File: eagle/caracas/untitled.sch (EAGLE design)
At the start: 24 parts, among them IC1 4001N, Q1 IRLZ44Z, X1 22-23-2021, X2 22-23-2021, X3 22-23-2021, X4 22-23-2041, X5 22-23-2021, X6 22-23-2041

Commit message: Possibly last version of schematics.
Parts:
- removed R6, R7, R8: 330, rcl:R-EU_0207/10
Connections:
- net +5V_SW_GND: now also X4-1.S
- net GND: now also U$1G$2.P$1; no longer R6.2, R7.2, R8.2, X4-1.S
- net N$10: now also X4-4.S; no longer R8.1, X4-2.S
- net N$7: now also X4-2.S; no longer R6.1, X4-4.S
- net N$8: no longer R7.1
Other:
- moved on the sheet: X4-1, X4-2, X4-3, X4-4
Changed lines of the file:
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@@
 <class number="0" name="default" width="0" drill="0">
 </class>
-<class number="1" name="Ground" width="0.6096" drill="0">
+<class number="1" name="Ground" width="0.4064" drill="0">
 <clearance class="1" value="0.3048"/>
 </class>
@@
 <part name="R10" library="rcl" deviceset="R-EU_" device="0207/10" value="1k"/>
 <part name="R9" library="rcl" deviceset="R-EU_" device="0207/10" value="1k"/>
-<part name="R6" library="rcl" deviceset="R-EU_" device="0207/10" value="330"/>
-<part name="R7" library="rcl" deviceset="R-EU_" device="0207/10" value="330"/>
-<part name="R8" library="rcl" deviceset="R-EU_" device="0207/10" value="330"/>
 <part name="X2" library="con-molex" deviceset="22-23-2021" device=""/>
 <part name="X3" library="con-molex" deviceset="22-23-2021" device=""/>
@@
 <instance part="R10" gate="G$1" x="-38.1" y="27.94" rot="R180"/>
 <instance part="R9" gate="G$1" x="-38.1" y="25.4" rot="R180"/>
-<instance part="R6" gate="G$1" x="-114.3" y="20.32" rot="R180"/>
-<instance part="R7" gate="G$1" x="-114.3" y="22.86" rot="R180"/>
-<instance part="R8" gate="G$1" x="-114.3" y="25.4" rot="R180"/>
 <instance part="X2" gate="-1" x="-213.36" y="12.7" rot="R90"/>
 <instance part="X2" gate="-2" x="-210.82" y="12.7" rot="R90"/>
@@
 <instance part="X1" gate="-2" x="-220.98" y="-55.88" rot="R270"/>
 <instance part="X6" gate="-1" x="-45.72" y="48.26" rot="R90"/>
-<instance part="X4" gate="-2" x="-99.06" y="0" rot="R270"/>
-<instance part="X4" gate="-3" x="-101.6" y="0" rot="R270"/>
-<instance part="X4" gate="-4" x="-104.14" y="0" rot="R270"/>
-<instance part="X4" gate="-1" x="-203.2" y="-55.88" rot="R270"/>
+<instance part="X4" gate="-2" x="-111.76" y="20.32" rot="R180"/>
+<instance part="X4" gate="-3" x="-111.76" y="22.86" rot="R180"/>
+<instance part="X4" gate="-4" x="-111.76" y="25.4" rot="R180"/>
 <instance part="X6" gate="-4" x="-25.4" y="17.78" rot="R270"/>
 <instance part="X6" gate="-3" x="-27.94" y="17.78" rot="R270"/>
@@
 <instance part="T1" gate="G$1" x="-152.4" y="-22.86"/>
 <instance part="R2" gate="G$1" x="-165.1" y="-22.86"/>
+<instance part="X4" gate="-1" x="-111.76" y="17.78" rot="R180"/>
+<instance part="U$1" gate="G$2" x="-223.52" y="-58.42" rot="R270"/>
 </instances>
 <busses>
@@
 <segment>
 <pinref part="U$1" gate="G$1" pin="P$1"/>
-<wire x1="-228.6" y1="-53.34" x2="-220.98" y2="-53.34" width="0.1524" layer="91"/>
+<wire x1="-228.6" y1="-53.34" x2="-223.52" y2="-53.34" width="0.1524" layer="91"/>
 <pinref part="X3" gate="-1" pin="S"/>
+<wire x1="-223.52" y1="-53.34" x2="-220.98" y2="-53.34" width="0.1524" layer="91"/>
 <wire x1="-220.98" y1="-53.34" x2="-218.44" y2="-53.34" width="0.1524" layer="91"/>
 <wire x1="-218.44" y1="-53.34" x2="-210.82" y2="-53.34" width="0.1524" layer="91"/>
 <wire x1="-210.82" y1="-53.34" x2="-208.28" y2="-53.34" width="0.1524" layer="91"/>
-<wire x1="-208.28" y1="-53.34" x2="-203.2" y2="-53.34" width="0.1524" layer="91"/>
 <junction x="-208.28" y="-53.34"/>
 <pinref part="X3" gate="-2" pin="S"/>
@@
 <junction x="-220.98" y="-53.34"/>
 <pinref part="IC1" gate="P" pin="VSS"/>
-<wire x1="-198.12" y1="-53.34" x2="-203.2" y2="-53.34" width="0.1524" layer="91"/>
+<wire x1="-198.12" y1="-53.34" x2="-208.28" y2="-53.34" width="0.1524" layer="91"/>
 <wire x1="-198.12" y1="-30.48" x2="-198.12" y2="-53.34" width="0.1524" layer="91"/>
 <junction x="-198.12" y="-53.34"/>
-<pinref part="X4" gate="-1" pin="S"/>
-<junction x="-203.2" y="-53.34"/>
 <pinref part="SUPPLY2" gate="GND" pin="GND"/>
 <pinref part="D1" gate="1" pin="A"/>
@@
 <pinref part="Q1" gate="G$1" pin="S"/>
 <wire x1="-91.44" y1="-15.24" x2="-91.44" y2="-53.34" width="0.1524" layer="91"/>
-<wire x1="-91.44" y1="-53.34" x2="-134.62" y2="-53.34" width="0.1524" layer="91"/>
+<wire x1="-91.44" y1="-53.34" x2="-142.24" y2="-53.34" width="0.1524" layer="91"/>
 <junction x="-142.24" y="-53.34"/>
 <pinref part="T1" gate="G$1" pin="E"/>
-<wire x1="-134.62" y1="-53.34" x2="-142.24" y2="-53.34" width="0.1524" layer="91"/>
 <wire x1="-149.86" y1="-27.94" x2="-149.86" y2="-53.34" width="0.1524" layer="91"/>
 <junction x="-149.86" y="-53.34"/>
-<wire x1="-203.2" y1="-53.34" x2="-177.8" y2="-53.34" width="0.1524" layer="91"/>
+<wire x1="-198.12" y1="-53.34" x2="-177.8" y2="-53.34" width="0.1524" layer="91"/>
 <pinref part="MCP3008" gate="A" pin="DGND"/>
 <wire x1="-17.78" y1="2.54" x2="-22.86" y2="2.54" width="0.1524" layer="91"/>
@@
 <wire x1="-22.86" y1="-53.34" x2="-91.44" y2="-53.34" width="0.1524" layer="91"/>
 <junction x="-91.44" y="-53.34"/>
-<pinref part="R8" gate="G$1" pin="2"/>
-<wire x1="-119.38" y1="25.4" x2="-134.62" y2="25.4" width="0.1524" layer="91"/>
-<pinref part="R6" gate="G$1" pin="2"/>
-<wire x1="-119.38" y1="20.32" x2="-134.62" y2="20.32" width="0.1524" layer="91"/>
-<wire x1="-134.62" y1="20.32" x2="-134.62" y2="22.86" width="0.1524" layer="91"/>
-<wire x1="-134.62" y1="22.86" x2="-134.62" y2="25.4" width="0.1524" layer="91"/>
-<pinref part="R7" gate="G$1" pin="2"/>
-<wire x1="-119.38" y1="22.86" x2="-134.62" y2="22.86" width="0.1524" layer="91"/>
-<junction x="-134.62" y="22.86"/>
-<junction x="-134.62" y="20.32"/>
-<wire x1="-134.62" y1="20.32" x2="-134.62" y2="-53.34" width="0.1524" layer="91"/>
-<junction x="-134.62" y="-53.34"/>
+<pinref part="U$1" gate="G$2" pin="P$1"/>
+<junction x="-223.52" y="-53.34"/>
 </segment>
 </net>
@@
 <pinref part="Q1" gate="G$1" pin="D"/>
 <wire x1="-91.44" y1="17.78" x2="-91.44" y2="-5.08" width="0.1524" layer="91"/>
+<pinref part="X4" gate="-1" pin="S"/>
+<wire x1="-109.22" y1="17.78" x2="-91.44" y2="17.78" width="0.1524" layer="91"/>
+<junction x="-91.44" y="17.78"/>
 </segment>
 </net>
@@
 <segment>
 <pinref part="RASPBERRYPI" gate="A" pin="8"/>
-<wire x1="-81.28" y1="20.32" x2="-104.14" y2="20.32" width="0.1524" layer="91"/>
-<wire x1="-104.14" y1="20.32" x2="-109.22" y2="20.32" width="0.1524" layer="91"/>
-<wire x1="-104.14" y1="20.32" x2="-104.14" y2="2.54" width="0.1524" layer="91"/>
-<junction x="-104.14" y="20.32"/>
-<pinref part="R6" gate="G$1" pin="1"/>
+<wire x1="-81.28" y1="20.32" x2="-109.22" y2="20.32" width="0.1524" layer="91"/>
+<pinref part="X4" gate="-2" pin="S"/>
+</segment>
+</net>
+<net name="N$8" class="0">
+<segment>
+<pinref part="RASPBERRYPI" gate="A" pin="10"/>
+<wire x1="-81.28" y1="22.86" x2="-109.22" y2="22.86" width="0.1524" layer="91"/>
+<pinref part="X4" gate="-3" pin="S"/>
+</segment>
+</net>
+<net name="N$10" class="0">
+<segment>
+<pinref part="RASPBERRYPI" gate="A" pin="12"/>
+<wire x1="-81.28" y1="25.4" x2="-109.22" y2="25.4" width="0.1524" layer="91"/>
 <pinref part="X4" gate="-4" pin="S"/>
 </segment>
 </net>
-<net name="N$8" class="0">
-<segment>
-<pinref part="RASPBERRYPI" gate="A" pin="10"/>
-<wire x1="-81.28" y1="22.86" x2="-101.6" y2="22.86" width="0.1524" layer="91"/>
-<wire x1="-104.14" y1="22.86" x2="-101.6" y2="22.86" width="0.1524" layer="91"/>
-<wire x1="-101.6" y1="22.86" x2="-109.22" y2="22.86" width="0.1524" layer="91"/>
-<wire x1="-101.6" y1="22.86" x2="-101.6" y2="2.54" width="0.1524" layer="91"/>
-<junction x="-101.6" y="22.86"/>
-<pinref part="R7" gate="G$1" pin="1"/>
-<pinref part="X4" gate="-3" pin="S"/>
-</segment>
-</net>
-<net name="N$10" class="0">
-<segment>
-<pinref part="RASPBERRYPI" gate="A" pin="12"/>
-<wire x1="-81.28" y1="25.4" x2="-99.06" y2="25.4" width="0.1524" layer="91"/>
-<wire x1="-99.06" y1="25.4" x2="-109.22" y2="25.4" width="0.1524" layer="91"/>
-<wire x1="-99.06" y1="2.54" x2="-99.06" y2="25.4" width="0.1524" layer="91"/>
-<junction x="-99.06" y="25.4"/>
-<pinref part="R8" gate="G$1" pin="1"/>
-<pinref part="X4" gate="-2" pin="S"/>
-</segment>
-</net>

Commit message: Schematics adjusted once again.
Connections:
- net +3.3V: no longer R10.2, R9.2
- net GND: now also R10.2, R9.2
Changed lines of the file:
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@@
 <wire x1="-17.78" y1="5.08" x2="-22.86" y2="5.08" width="0.1524" layer="91"/>
 <wire x1="-22.86" y1="2.54" x2="-22.86" y2="-53.34" width="0.1524" layer="91"/>
-<wire x1="-22.86" y1="-53.34" x2="-91.44" y2="-53.34" width="0.1524" layer="91"/>
+<wire x1="-22.86" y1="-53.34" x2="-45.72" y2="-53.34" width="0.1524" layer="91"/>
 <junction x="-91.44" y="-53.34"/>
 <pinref part="U$1" gate="G$2" pin="P$1"/>
 <junction x="-223.52" y="-53.34"/>
+<pinref part="R9" gate="G$1" pin="2"/>
+<wire x1="-45.72" y1="-53.34" x2="-91.44" y2="-53.34" width="0.1524" layer="91"/>
+<wire x1="-43.18" y1="25.4" x2="-45.72" y2="25.4" width="0.1524" layer="91"/>
+<wire x1="-45.72" y1="25.4" x2="-45.72" y2="-53.34" width="0.1524" layer="91"/>
+<pinref part="R10" gate="G$1" pin="2"/>
+<wire x1="-43.18" y1="27.94" x2="-45.72" y2="27.94" width="0.1524" layer="91"/>
+<wire x1="-45.72" y1="27.94" x2="-45.72" y2="25.4" width="0.1524" layer="91"/>
+<junction x="-45.72" y="25.4"/>
 </segment>
 </net>
@@
 <pinref part="MCP3008" gate="A" pin="VREF"/>
 <wire x1="-17.78" y1="43.18" x2="-48.26" y2="43.18" width="0.1524" layer="91"/>
-<wire x1="-43.18" y1="27.94" x2="-48.26" y2="27.94" width="0.1524" layer="91"/>
-<pinref part="R10" gate="G$1" pin="2"/>
-<wire x1="-48.26" y1="25.4" x2="-43.18" y2="25.4" width="0.1524" layer="91"/>
-<pinref part="R9" gate="G$1" pin="2"/>
-<junction x="-48.26" y="27.94"/>
 <junction x="-48.26" y="43.18"/>
 <pinref part="X6" gate="-2" pin="S"/>
@@
 <pinref part="X6" gate="-1" pin="S"/>
 <junction x="-45.72" y="45.72"/>
-<wire x1="-48.26" y1="12.7" x2="-48.26" y2="25.4" width="0.1524" layer="91"/>
-<wire x1="-48.26" y1="25.4" x2="-48.26" y2="27.94" width="0.1524" layer="91"/>
-<wire x1="-48.26" y1="27.94" x2="-48.26" y2="43.18" width="0.1524" layer="91"/>
+<wire x1="-48.26" y1="12.7" x2="-48.26" y2="43.18" width="0.1524" layer="91"/>
 <wire x1="-48.26" y1="43.18" x2="-48.26" y2="45.72" width="0.1524" layer="91"/>
-<junction x="-48.26" y="25.4"/>
 </segment>
 </net>

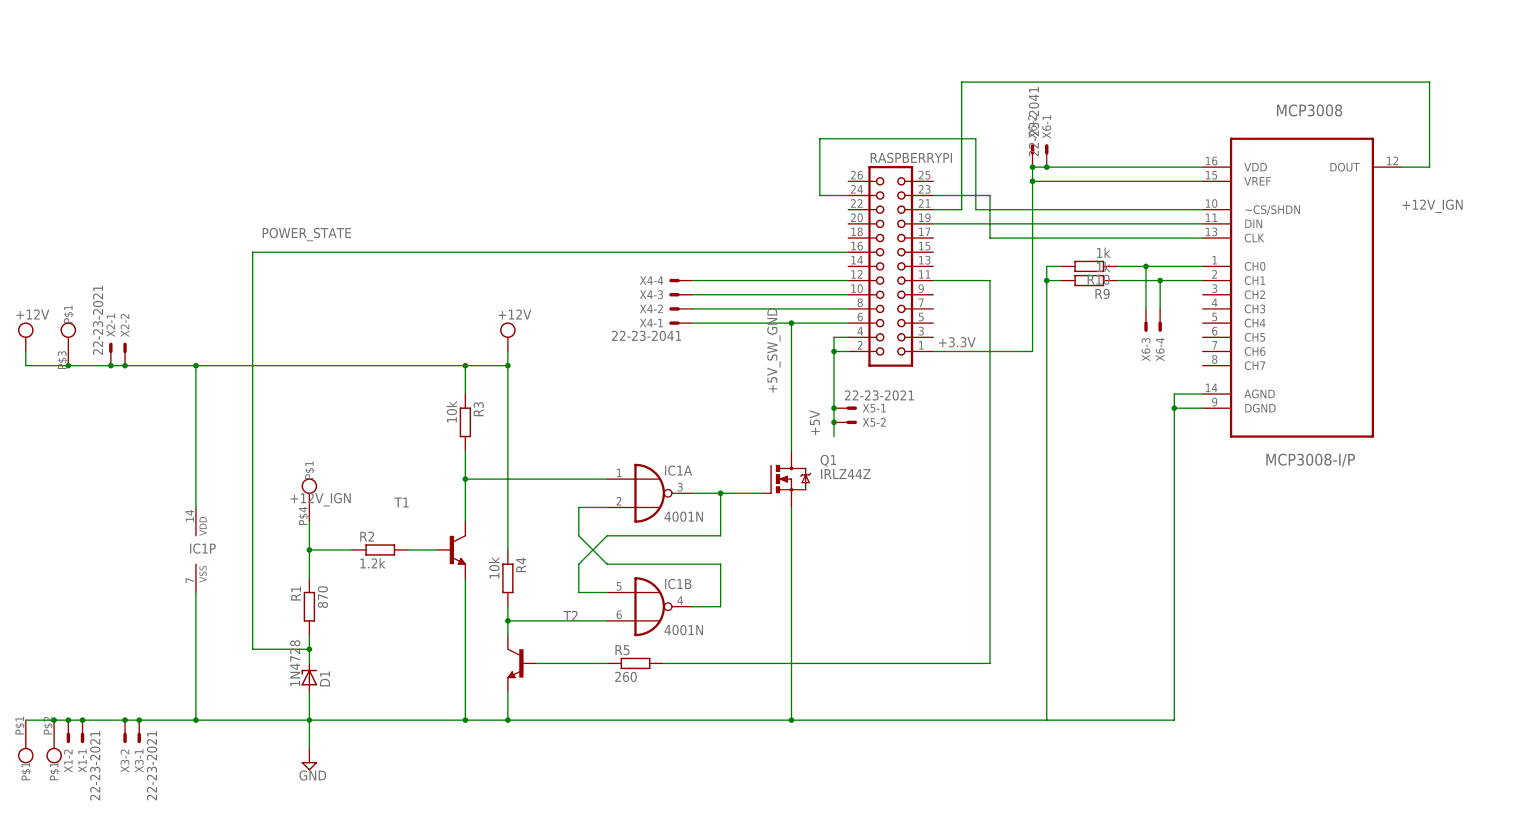
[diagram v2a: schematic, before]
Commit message: Refactor hardware board into a Raspberry PI B+ compatible HAT board
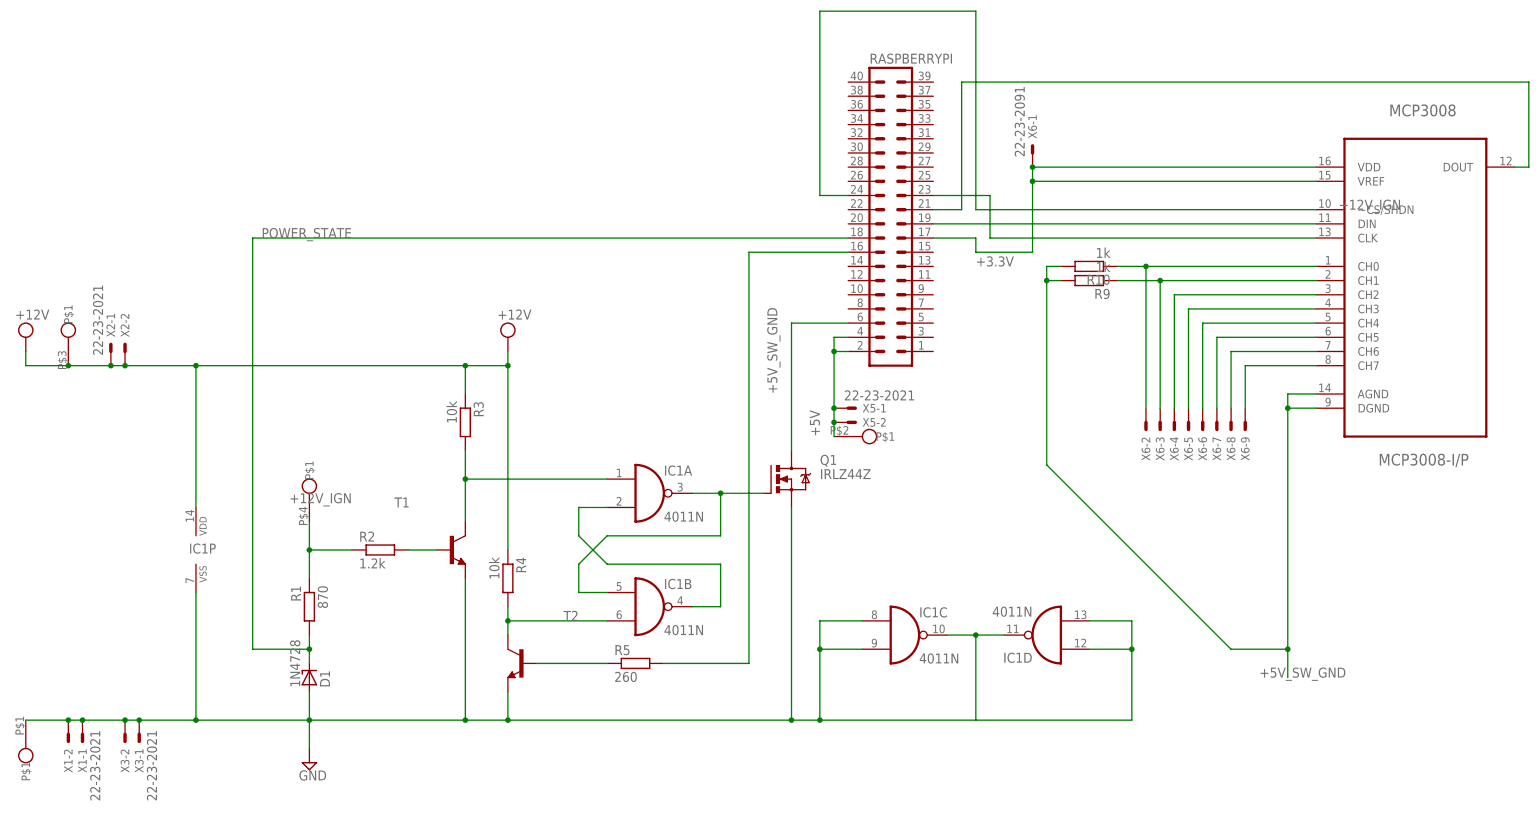
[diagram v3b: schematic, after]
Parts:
- removed X4: 22-23-2041, con-molex:22-23-2041
- IC1: value 4001N -> 4011N; device 40xx:4001N -> 40xx:4011N
- RASPBERRYPI: device con-harting:CON26 -> con-lstb:MA20-2
- X6: value 22-23-2041 -> 22-23-2091; device con-molex:22-23-2041 -> con-molex:22-23-2091
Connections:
- removed net RPI_RESET: R5.2, RASPBERRYPI.11
- new net N$14: MCP3008.CH6, X6-8.S
- new net N$15: MCP3008.CH7, X6-9.S
- new net N$16: R5.2, RASPBERRYPI.16
- new net N$6: MCP3008.CH2, X6-4.S
- net +3.3V: now also RASPBERRYPI.17; no longer RASPBERRYPI.1, X6-2.S
- net +5V: now also U$1G$2.P$1
- net +5V_SW_GND: now also MCP3008.AGND, MCP3008.DGND, R10.2, R9.2; no longer X4-1.S
- net ANA_0: now also X6-2.S; no longer X6-3.S
- net ANA_1: now also X6-3.S; no longer X6-4.S
- net GND: now also IC1C.I0, IC1C.I1, IC1C.O, IC1D.I0, IC1D.I1, IC1D.O; no longer MCP3008.AGND, MCP3008.DGND, R10.2, R9.2, U$1G$2.P$1
- net N$10: now also MCP3008.CH5, X6-7.S; no longer RASPBERRYPI.12, X4-4.S
- net N$7: now also MCP3008.CH3, X6-5.S; no longer RASPBERRYPI.8, X4-2.S
- net N$8: now also MCP3008.CH4, X6-6.S; no longer RASPBERRYPI.10, X4-3.S
- net POWER_STATE: now also RASPBERRYPI.18; no longer RASPBERRYPI.16
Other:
- moved on the sheet: MCP3008, X6-1, X6-2, X6-3, X6-4

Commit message: Update schematics again
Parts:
- added C1: (no value), rcl:CPOL-USE2,5-6E
- added R6: 260, rcl:R-EU_0207/10
- added R7: 115, rcl:R-EU_0207/10
- added T3: (no value), transistor:BC547-NPN-TO92-CBE
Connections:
- new net N$18: R6.2, T3.B
- new net N$19: R6.1, RASPBERRYPI.32
- new net POWER_CONTROL: R7.2, T3.E, U$1G$2.P$1
- net +5V: now also C1.+; no longer U$1G$2.P$1
- net +5V_SW_GND: now also C1.-
- net GND: now also R7.1
- net VCC: now also T3.C
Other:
- moved on the sheet: IC1C, IC1D, MCP3008, R10, R9, RASPBERRYPI, X5-1, X5-2, X6-1, X6-2, X6-3, X6-4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

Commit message: Final board v2.0
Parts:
- C1: value (none) -> 0.1µ
- renumbered IC1 to 4011, RASPBERRYPI to RASPBERRY_PI_GPIO, X1 to GND_1, X2 to 12V_IN, X3 to GND_2, X5 to +5VOUT, X6 to ADC

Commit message: Power board v2 does not work, start working on v3
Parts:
- removed C1: 0.1µ, rcl:CPOL-USE2,5-6E
- removed D1: 1N4728, diode:1N4728
- removed T3: (no value), transistor:BC547-NPN-TO92-CBE
- removed U$1: MKDS3, caracas:MKDS3
- added EXT: MKDS3, caracas:MKDS3
- added Q2: IRF9530, transistor-fet:IRF9530
- added Q3: (no value), transistors:2N7000_SOT23
- added Q4: IRLML5203, transistor-power:IRLML5203
- added R11: 1k, rcl:R-EU_0204/5
- added R8: 10k, rcl:R-EU_0204/5
- Q1: value IRLZ44Z -> (none); device transistor-power:IRLZ44Z -> transistors:2N7000_SOT23
- R1: value 870 -> 10k; device rcl:R-EU_0207/10 -> rcl:R-EU_0204/5
- R10, R3: device rcl:R-EU_0207/10 -> rcl:R-EU_0204/5
- R2: value 1.2k -> 10k; device rcl:R-EU_0207/10 -> rcl:R-EU_0204/5
- R4: value 10k -> 1.2k
- R5, R6: value 260 -> 10k; device rcl:R-EU_0207/10 -> rcl:R-EU_0204/5
- R7: value 115 -> 260
- renumbered MCP3008 to MCP1
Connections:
- removed net +5V_SW_GND: C1.-, MCP1.AGND, MCP1.DGND, Q1.D, R10.2, R9.2, RASPBERRY_PI_GPIO.6
- removed net POWER_CONTROL: R7.2, T3.E, U$1G$2.P$1
- new net N$17: Q2.D, RASPBERRY_PI_GPIO.2, RASPBERRY_PI_GPIO.4
- new net N$21: Q1.D, R1.2
- new net N$22: Q3.D, Q4.G, R9.1
- new net PWR_CTRL: EXTG$2.P$1, Q4.D
- net +12V_IGN: now also EXTG$4.P$1, R2.2, R3.2, R4.1; no longer R1.1, R2.1, U$1G$4.P$1
- net +5V: now also Q2.S; no longer C1.+, RASPBERRY_PI_GPIO.2, RASPBERRY_PI_GPIO.4
- net ANA_0: now also R11.1; no longer R10.1
- net ANA_1: now also R10.1; no longer R9.1
- net GND: now also EXTG$1.P$1, MCP1.AGND, MCP1.DGND, Q3.S, R10.2, R11.2, R3.1, R8.1, RASPBERRY_PI_GPIO.6; no longer 4011C.O, 4011D.O, D1.A, R7.1, U$1G$1.P$1
- net MOSFET_ON: now also Q2.G
- net N$1: no longer Q1.G
- net N$11: now also R5.2; no longer R3.2
- net N$12: now also R4.2; no longer R2.2
- net N$16: now also R7.2; no longer R5.2
- net N$18: now also Q1.G, R2.1; no longer R6.2, T3.B
- net N$19: now also Q3.G, R8.2; no longer R6.1
- net N$2: now also R6.2; no longer R4.2
- net N$9: now also R7.1; no longer R5.1
- net POWER_STATE: now also R1.1; no longer D1.C, R1.2
- net VCC: now also EXTG$3.P$1, Q4.S, R5.1, R6.1, R9.2; no longer R3.1, R4.1, T3.C, U$1G$3.P$1
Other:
- moved on the sheet: +5VOUT-1, +5VOUT-2, 12V_IN-1, 12V_IN-2, 4011C, 4011D, 4011P, GND_1-1, GND_1-2, GND_2-1, GND_2-2, R1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

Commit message: More schematics WIP
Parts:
- removed Q4: IRLML5203, transistor-power:IRLML5203
- removed T1, T2: (no value), transistor:BC547-NPN-TO92-CBE
- Q1: value (none) -> AO4842; device transistors:2N7000_SOT23 -> caracas:AO4842
- Q2: value IRF9530 -> AO4842; device transistor-fet:IRF9530 -> caracas:AO4842
- Q3: value (none) -> AO4807; device transistors:2N7000_SOT23 -> caracas:AO4807
- R1, R10, R11, R2, R3, R5, R6, R8: device rcl:R-EU_0204/5 -> rcl:R-EU_0207/10
- R4: value 1.2k -> 10k
- R7: value 260 -> 10k
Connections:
- removed net N$16: R7.2, RASPBERRY_PI_GPIO.16
- removed net N$9: R7.1, T2.B
- new net SUICIDE_SIGNAL: Q1B.G, R7.2, RASPBERRY_PI_GPIO.16
- net +5V: now also Q3B.S; no longer Q2.S
- net ANA_0: now also R10.1; no longer R11.1
- net ANA_1: now also R11.1; no longer R10.1
- net GND: now also Q1A.S, Q1B.S, Q2A.S, Q2B.S, R7.1; no longer Q1.S, Q3.S, T1.E, T2.E
- net MOSFET_ON: now also Q3B.G; no longer Q2.G
- net N$11: now also Q1A.D; no longer T1.C
- net N$12: now also Q1A.G; no longer T1.B
- net N$17: now also Q3B.D; no longer Q2.D
- net N$18: now also Q2B.G; no longer Q1.G
- net N$19: now also Q2A.G; no longer Q3.G
- net N$2: now also Q1B.D; no longer T2.C
- net N$21: now also Q2B.D; no longer Q1.D
- net N$22: now also Q2A.D, Q3A.G; no longer Q3.D, Q4.G
- net PWR_CTRL: now also Q3A.D; no longer Q4.D
- net VCC: now also Q3A.S; no longer Q4.S
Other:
- note added: "Amplifier power on/off"
- note added: "S/R Latch circuit"
- moved on the sheet: +5VOUT-1, +5VOUT-2, 12V_IN-1, 12V_IN-2, 4011A, 4011B, 4011C, 4011D, 4011P, GND_1-1, GND_1-2, GND_2-1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

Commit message: Complete rework of the PCB
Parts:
- added R12, R13, R14, R15, R16, R17: 1k, rcl:R-EU_0207/10
- renumbered MCP1 to MCP3008
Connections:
- removed net GND: 4011C.I0, 4011C.I1, 4011D.I0, 4011D.I1, 4011P.VSS, EXTG$1.P$1, GND_1-1.S, GND_1-2.S, GND_2-1.S, GND_2-2.S, MCP3008.AGND, MCP3008.DGND, Q1A.S, Q1B.S, Q2A.S, Q2B.S, R10.2, R11.2, R3.1, R7.1, R8.1, RASPBERRY_PI_GPIO.6
- removed net N$19: Q2A.G, R8.2, RASPBERRY_PI_GPIO.32
- new net GND@BOTTOM: 4011C.I0, 4011C.I1, 4011D.I0, 4011D.I1, 4011P.VSS, EXTG$1.P$1, GND_1-1.S, GND_1-2.S, GND_2-1.S, GND_2-2.S, MCP3008.AGND, MCP3008.DGND, Q1A.S, Q1B.S, Q2A.S, Q2B.S, R10.1, R11.1, R12.1, R13.1, R14.1, R15.1, R16.1, R17.1, R3.1, R7.1, R8.1, RASPBERRY_PI_GPIO.9
- new net POWER_CONTROL: Q2A.G, R8.2, RASPBERRY_PI_GPIO.11
- net +12V_IGN: now also EXTG$3.P$1; no longer EXTG$4.P$1
- net ANA_0: now also R10.2; no longer R10.1
- net ANA_1: now also R11.2; no longer R11.1
- net N$10: now also R15.2
- net N$14: now also R16.2
- net N$15: now also R17.2
- net N$6: now also R12.2
- net N$7: now also R13.2
- net N$8: now also R14.2
- net PWR_CTRL: now also EXTG$4.P$1; no longer EXTG$2.P$1
- net VCC: now also EXTG$2.P$1; no longer EXTG$3.P$1
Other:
- moved on the sheet: 4011C, 4011D, ADC-2, ADC-3, ADC-4, ADC-5, ADC-6, ADC-7, ADC-8, ADC-9, R10, R11
